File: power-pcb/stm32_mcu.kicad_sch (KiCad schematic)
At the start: 37 parts, among them SW1 SW_Push, U6 STM32G474RBT6, Y1 8MHz

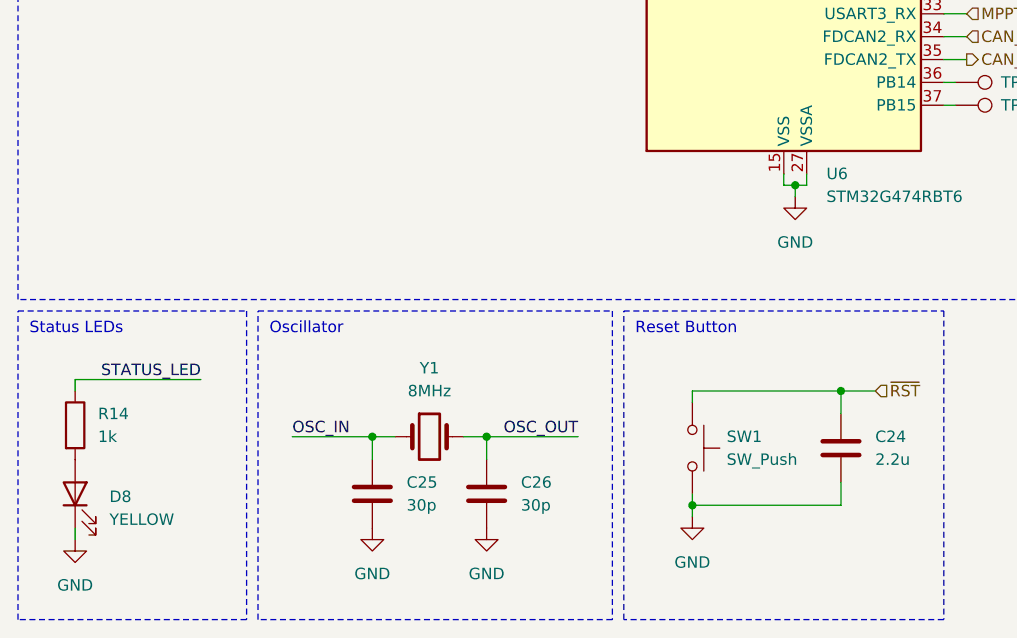
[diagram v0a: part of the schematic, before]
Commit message: power-pcb: re-annotate schematic and start board
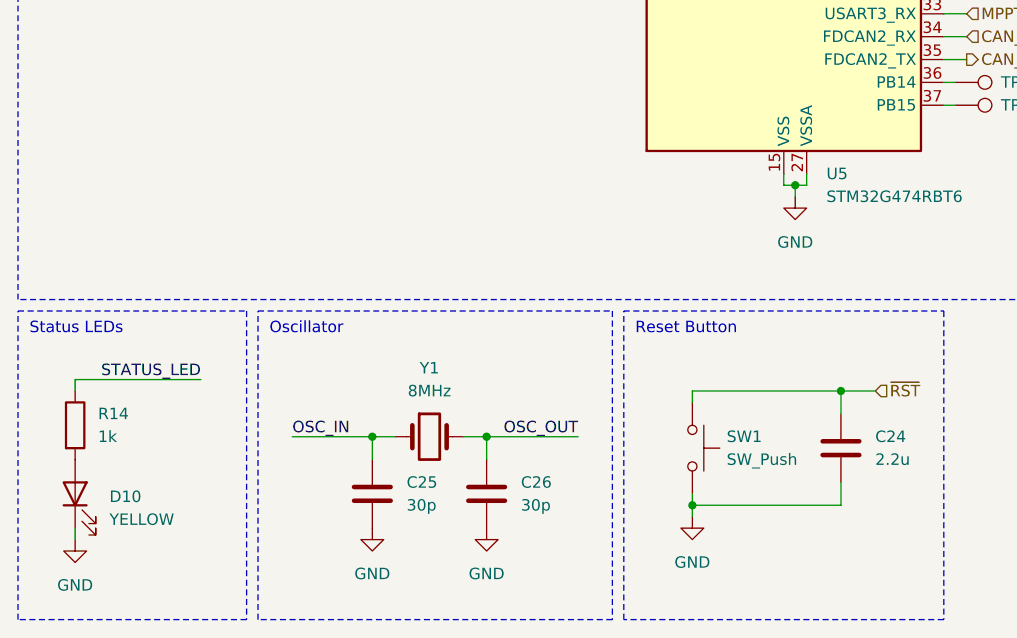
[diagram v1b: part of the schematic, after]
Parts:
- renumbered D8 to D10, U6 to U5
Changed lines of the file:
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@@
 		(dnp no)
 		(fields_autoplaced yes)
-		(property "Reference" "U6"
+		(property "Reference" "U5"
 			(at 102.5241 133.35 0)
 			(show_name no)
@@
 			(project "power-pcb"
 				(path "/4b4cf3aa-c94c-4150-b9c5-35049cd71136/7d59fd70-1fff-4c9c-ae77-583b08aef567"
-					(reference "U6")
+					(reference "U5")
 					(unit 1)
 					(variant
@@
 		(dnp no)
 		(fields_autoplaced yes)
-		(property "Reference" "D8"
+		(property "Reference" "D10"
 			(at 22.86 169.2274 90)
 			(show_name no)
@@
 			(project "power-pcb"
 				(path "/4b4cf3aa-c94c-4150-b9c5-35049cd71136/7d59fd70-1fff-4c9c-ae77-583b08aef567"
-					(reference "D8")
+					(reference "D10")
 					(unit 1)
 					(variant

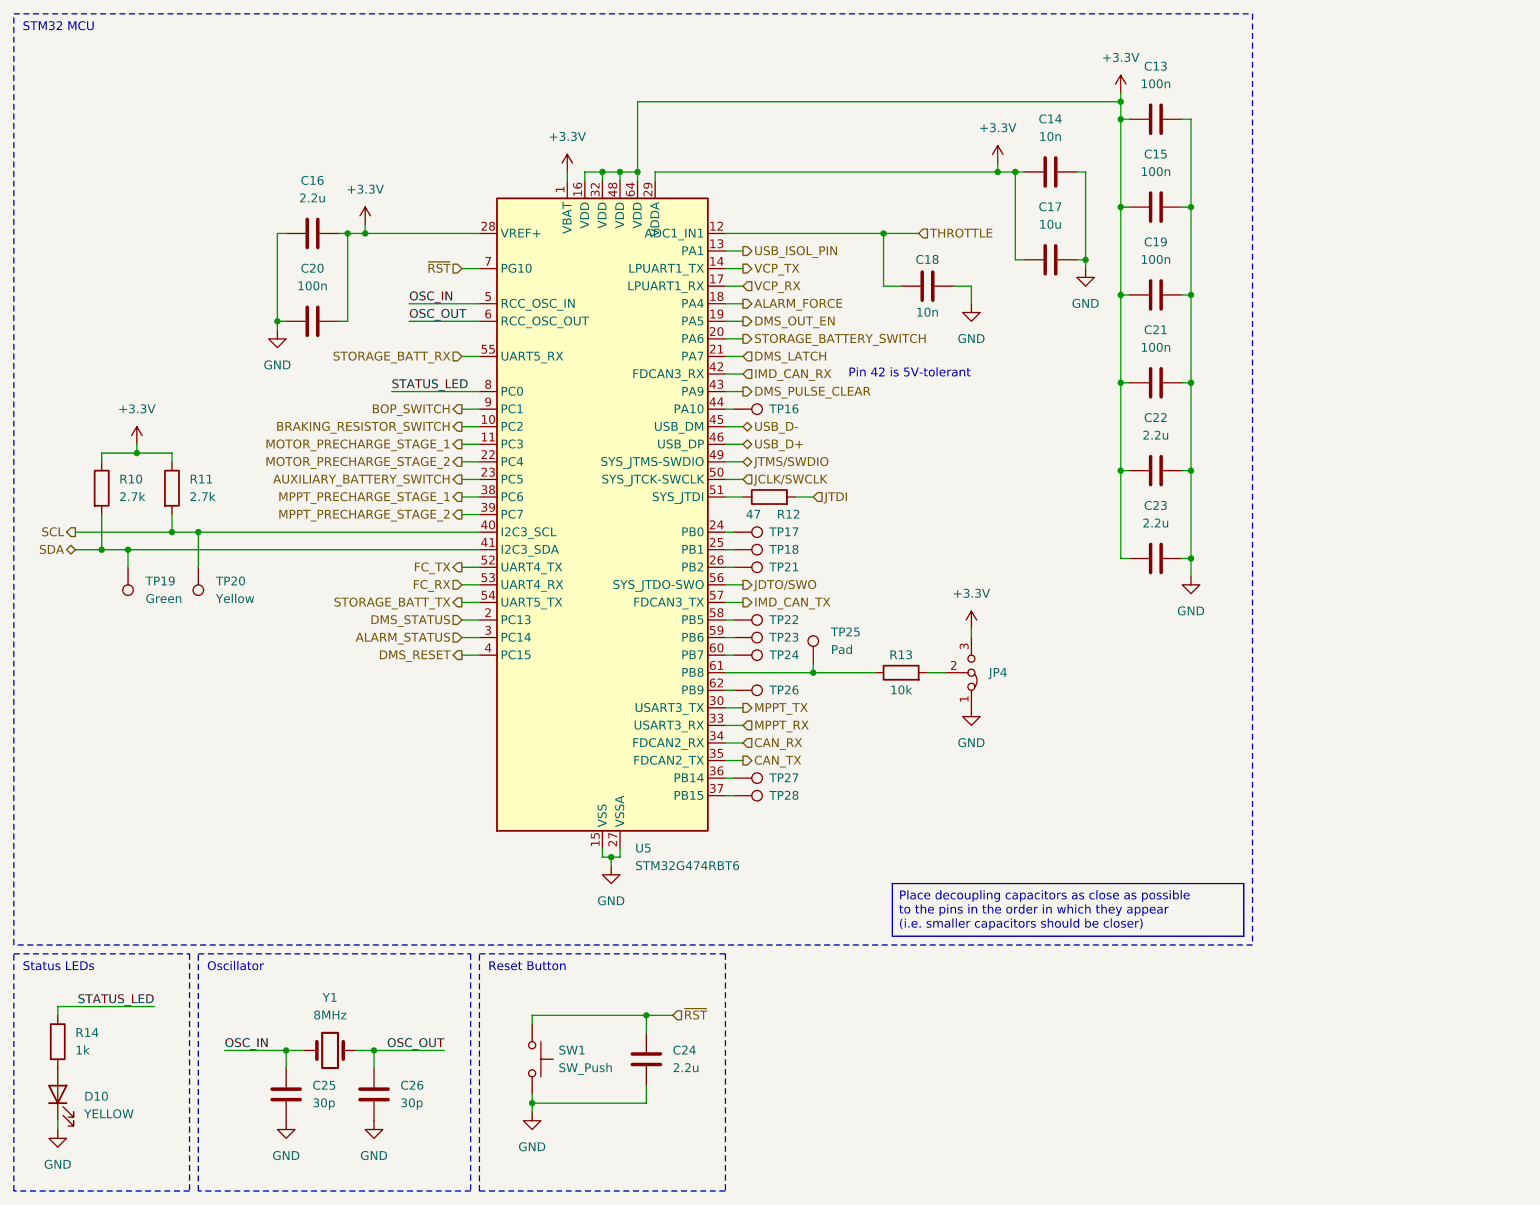
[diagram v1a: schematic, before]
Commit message: power-pcb: fix schematic after review
- Add footprint for resitive load for the RECOM
- Add Opamps when useful
- Add capacitor and change some footprint sizes
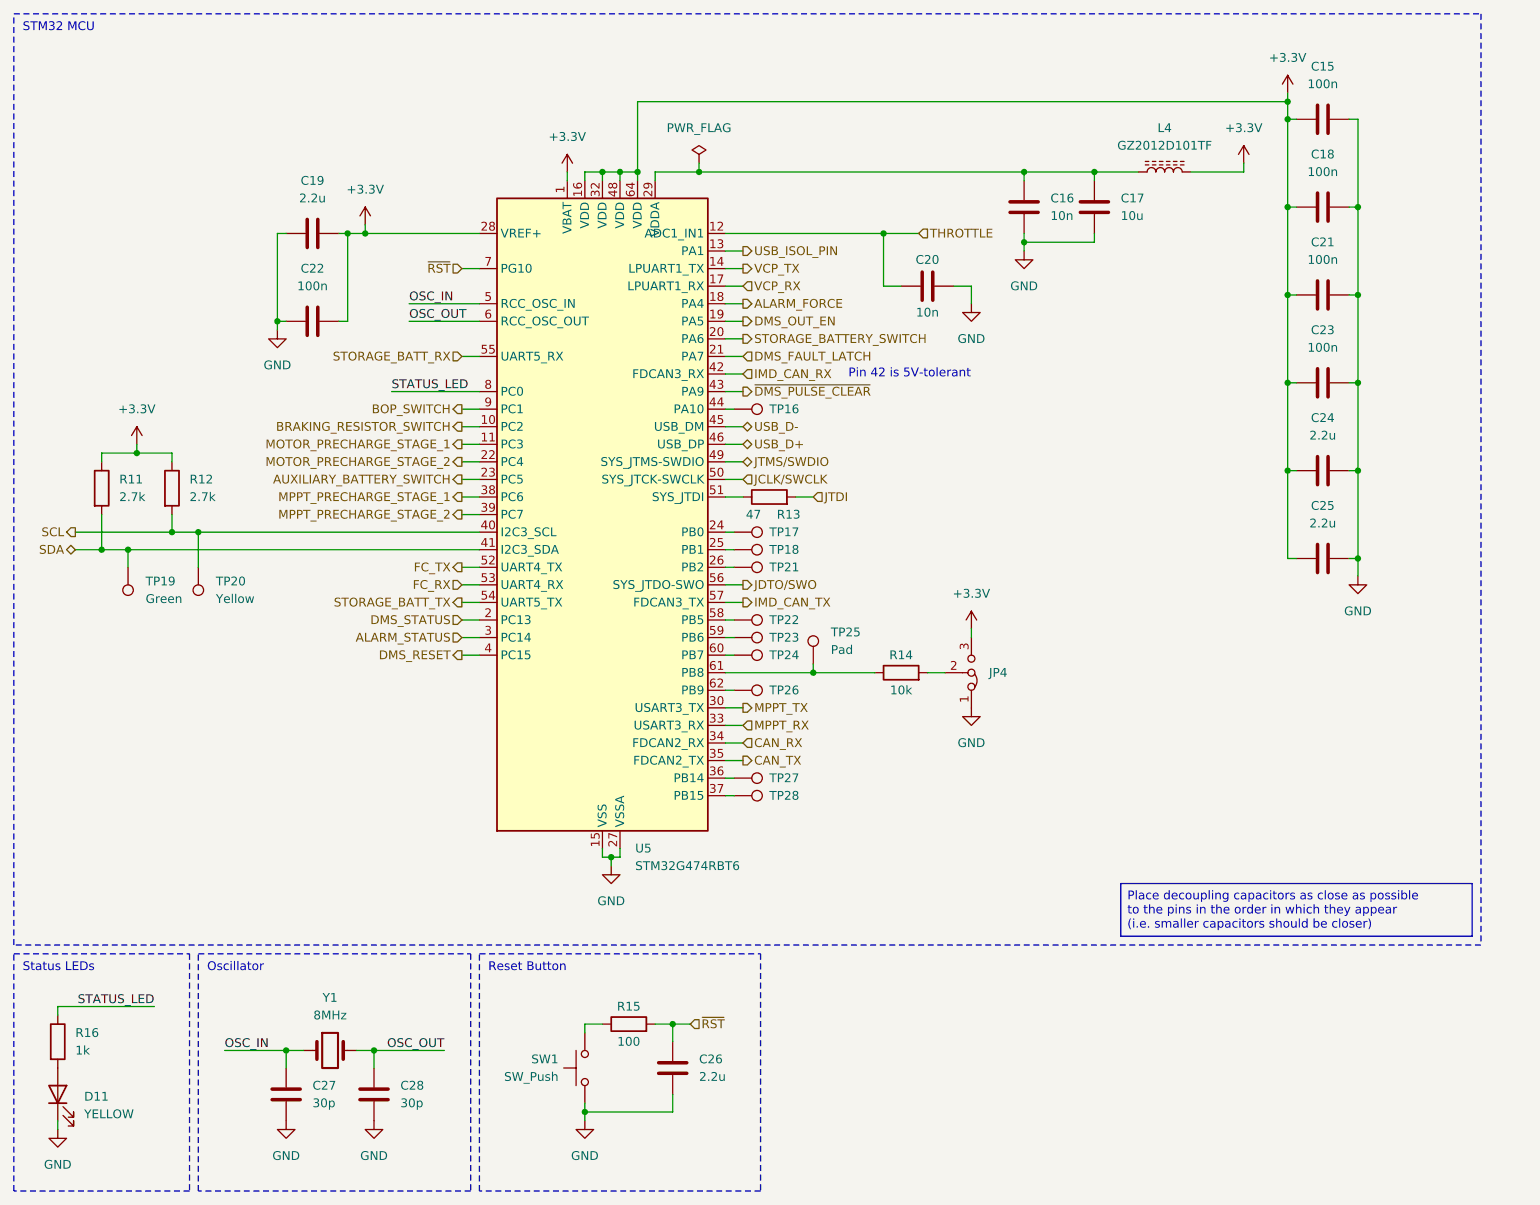
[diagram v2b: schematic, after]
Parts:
- added L4: GZ2012D101TF, Inductor_SMD:L_0805_2012Metric_Pad1.05x1.20mm_HandSolder, symbol Device:L_Ferrite
- added R15: 100, Resistor_SMD:R_0603_1608Metric_Pad0.98x0.95mm_HandSolder, symbol Device:R
- C15: renamed from C13; footprint Capacitor_SMD:C_0603_1608Metric_Pad1.08x0.95mm_HandSolder -> Capacitor_SMD:C_0402_1005Metric_Pad0.74x0.62mm_HandSolder; JLCPCB C14663 -> C307331
- C18: renamed from C15; footprint Capacitor_SMD:C_0603_1608Metric_Pad1.08x0.95mm_HandSolder -> Capacitor_SMD:C_0402_1005Metric_Pad0.74x0.62mm_HandSolder; JLCPCB C14663 -> C307331
- C21: renamed from C19; footprint Capacitor_SMD:C_0603_1608Metric_Pad1.08x0.95mm_HandSolder -> Capacitor_SMD:C_0402_1005Metric_Pad0.74x0.62mm_HandSolder; JLCPCB C14663 -> C307331
- C22: renamed from C20; footprint Capacitor_SMD:C_0603_1608Metric_Pad1.08x0.95mm_HandSolder -> Capacitor_SMD:C_0402_1005Metric_Pad0.74x0.62mm_HandSolder; JLCPCB C14663 -> C307331
- C23: renamed from C21; footprint Capacitor_SMD:C_0603_1608Metric_Pad1.08x0.95mm_HandSolder -> Capacitor_SMD:C_0402_1005Metric_Pad0.74x0.62mm_HandSolder; JLCPCB C14663 -> C307331
- renumbered C14 to C16, C16 to C19, C18 to C20, C22 to C24, C23 to C25, C24 to C26, C25 to C27, C26 to C28, D10 to D11, R10 to R11, R11 to R12, R12 to R13, R13 to R14, R14 to R16
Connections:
- net +3.3V: now also L4.2; no longer C16.1, C17.1, U5.29 (VDDA)
- net GND: now also C16.1, C17.1; no longer C16.2, C17.2
- net ~{RST}: now also R15.2; no longer SW1.1
- net DMS_LATCH renamed DMS_FAULT_LATCH
- net DMS_PULSE_CLEAR renamed ~{DMS_PULSE_CLEAR}
- new net: C16.2, C17.2, L4.1, U5.29 (VDDA)
- new net: R15.1, SW1.1
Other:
- moved on the sheet: C15, C16, C17, C18, C21, C23, C24, C25, C26, SW1

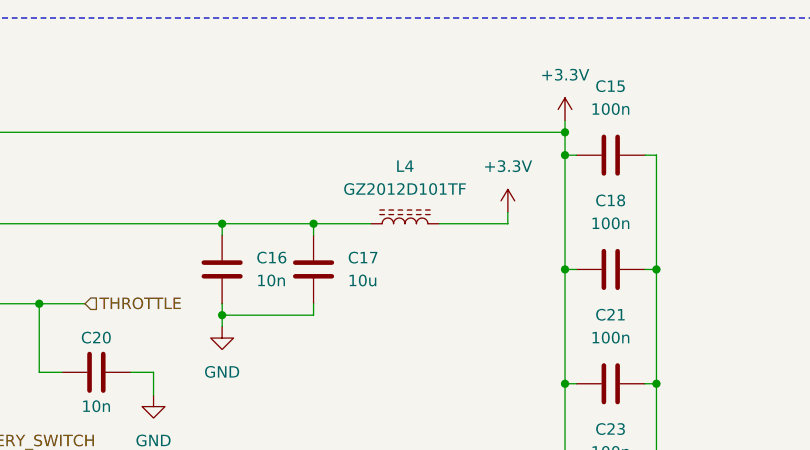
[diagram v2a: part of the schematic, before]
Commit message: power-pcb: work on part placement and JLCPCB DNP
Some of the components that were recentlt added had not been marked as
DNP for JLCPCB yet, this is now done.
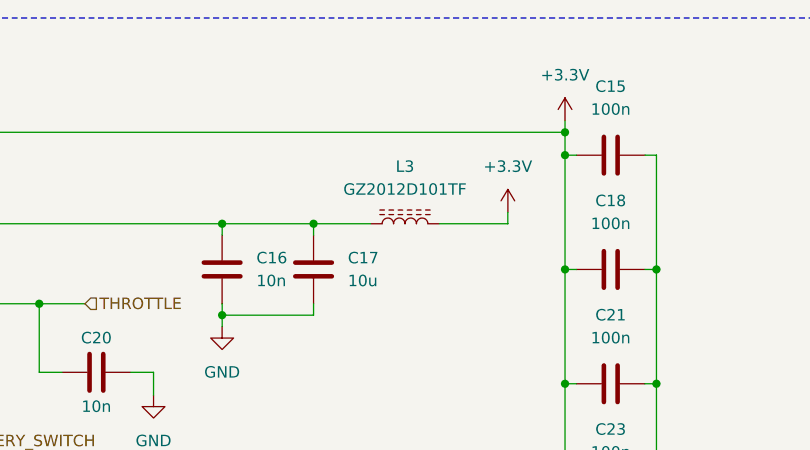
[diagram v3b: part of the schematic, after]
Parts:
- renumbered L4 to L3
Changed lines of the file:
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@@
 		(dnp no)
 		(fields_autoplaced yes)
-		(property "Reference" "L4"
+		(property "Reference" "L3"
 			(at 179.07 29.21 90)
 			(show_name no)
@@
 			(project "power-pcb"
 				(path "/4b4cf3aa-c94c-4150-b9c5-35049cd71136/7d59fd70-1fff-4c9c-ae77-583b08aef567"
-					(reference "L4")
+					(reference "L3")
 					(unit 1)
 					(variant
@@
 					(reference "R15")
 					(unit 1)
+					(variant
+						(name "JLCPCB")
+					)
 				)
 			)

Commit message: power-pcb: change some 10k to 12k
JLCPCB doesn't offer a small package for the 10k resistors so some had
to be changed.
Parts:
- R14: footprint Resistor_SMD:R_0603_1608Metric_Pad0.98x0.95mm_HandSolder -> Resistor_SMD:R_0805_2012Metric_Pad1.20x1.40mm_HandSolder; JLCPCB C25804 -> C17414
- R16: footprint Resistor_SMD:R_0402_1005Metric_Pad0.72x0.64mm_HandSolder -> Resistor_SMD:R_0603_1608Metric_Pad0.98x0.95mm_HandSolder; JLCPCB C11702 -> C21190
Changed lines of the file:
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@@
 	(title_block
 		(title "STM32 Microcontroller")
-		(date "2026-06-13")
+		(date "2026-06-19")
 		(rev "v1.1.0")
 	)
@@
 			)
 		)
-		(property "Footprint" "Resistor_SMD:R_0402_1005Metric_Pad0.72x0.64mm_HandSolder"
+		(property "Footprint" "Resistor_SMD:R_0603_1608Metric_Pad0.98x0.95mm_HandSolder"
 			(at 17.272 161.29 90)
 			(hide yes)
@@
 			)
 		)
-		(property "JLCPCB" "C11702"
+		(property "JLCPCB" "C21190"
 			(at 19.05 161.29 0)
 			(hide yes)
@@
 			)
 		)
-		(property "Footprint" "Resistor_SMD:R_0603_1608Metric_Pad0.98x0.95mm_HandSolder"
+		(property "Footprint" "Resistor_SMD:R_0805_2012Metric_Pad1.20x1.40mm_HandSolder"
 			(at 140.97 109.728 90)
 			(hide yes)
@@
 			)
 		)
-		(property "JLCPCB" "C25804"
+		(property "JLCPCB" "C17414"
 			(at 140.97 107.95 0)
 			(hide yes)
